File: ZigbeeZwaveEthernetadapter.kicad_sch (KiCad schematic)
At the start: 10 parts, among them J1 Barrel_Jack, J11 Conn_02x06_Odd_Even, J12 Conn_01x06, J14 Conn_01x06, J2 USB_B_Micro, J21 Conn_02x05_Odd_Even, J3 USB_C_Receptacle_USB2.0, U1 L7805

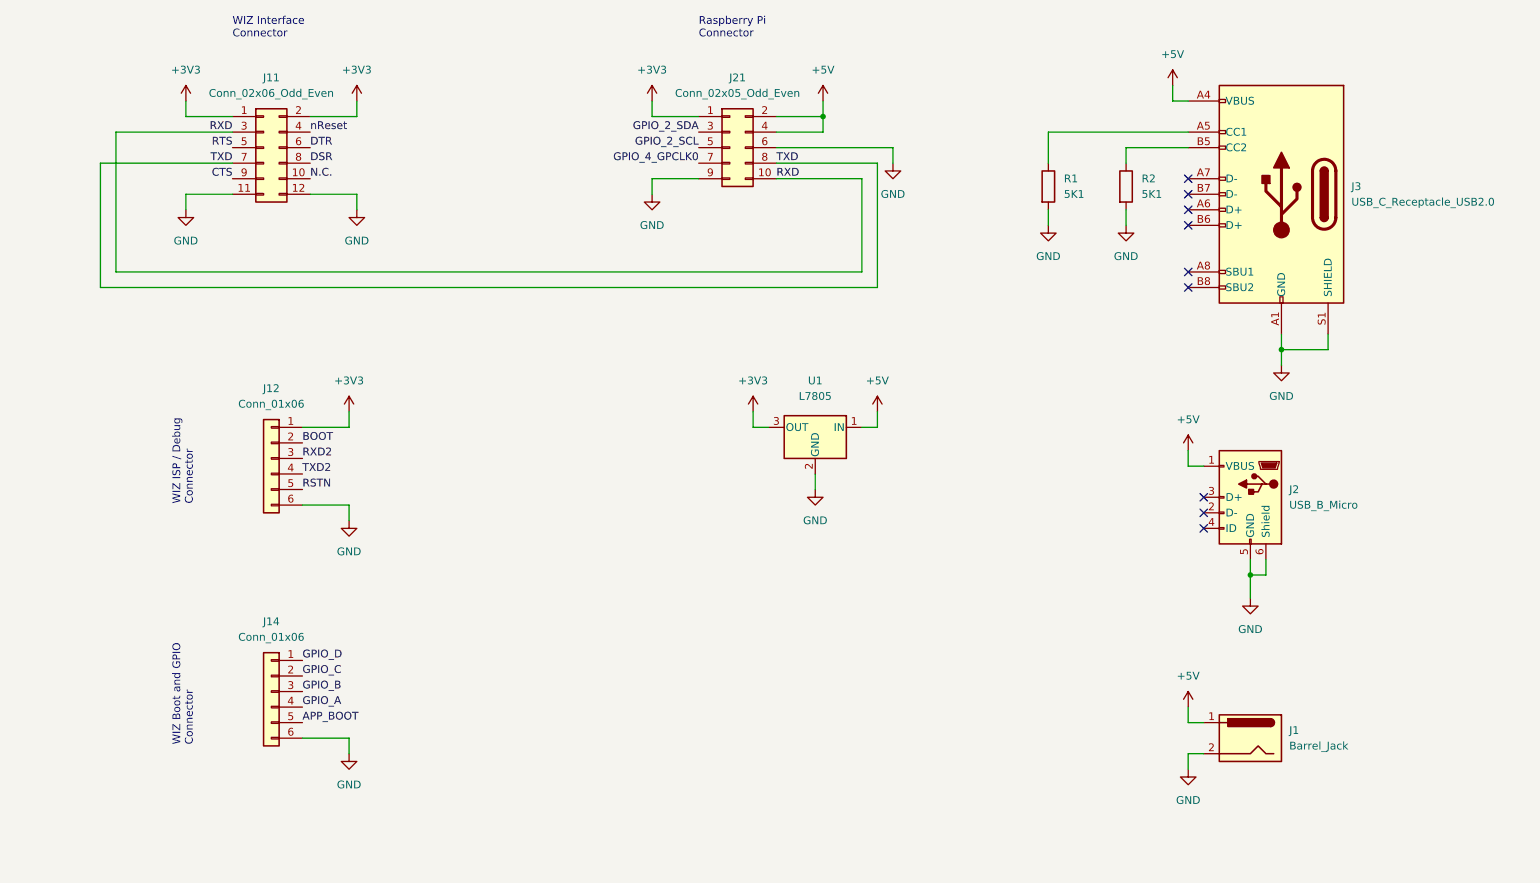
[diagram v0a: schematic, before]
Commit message: Mod: Finished schematic, changed linear regulator and added second pinout
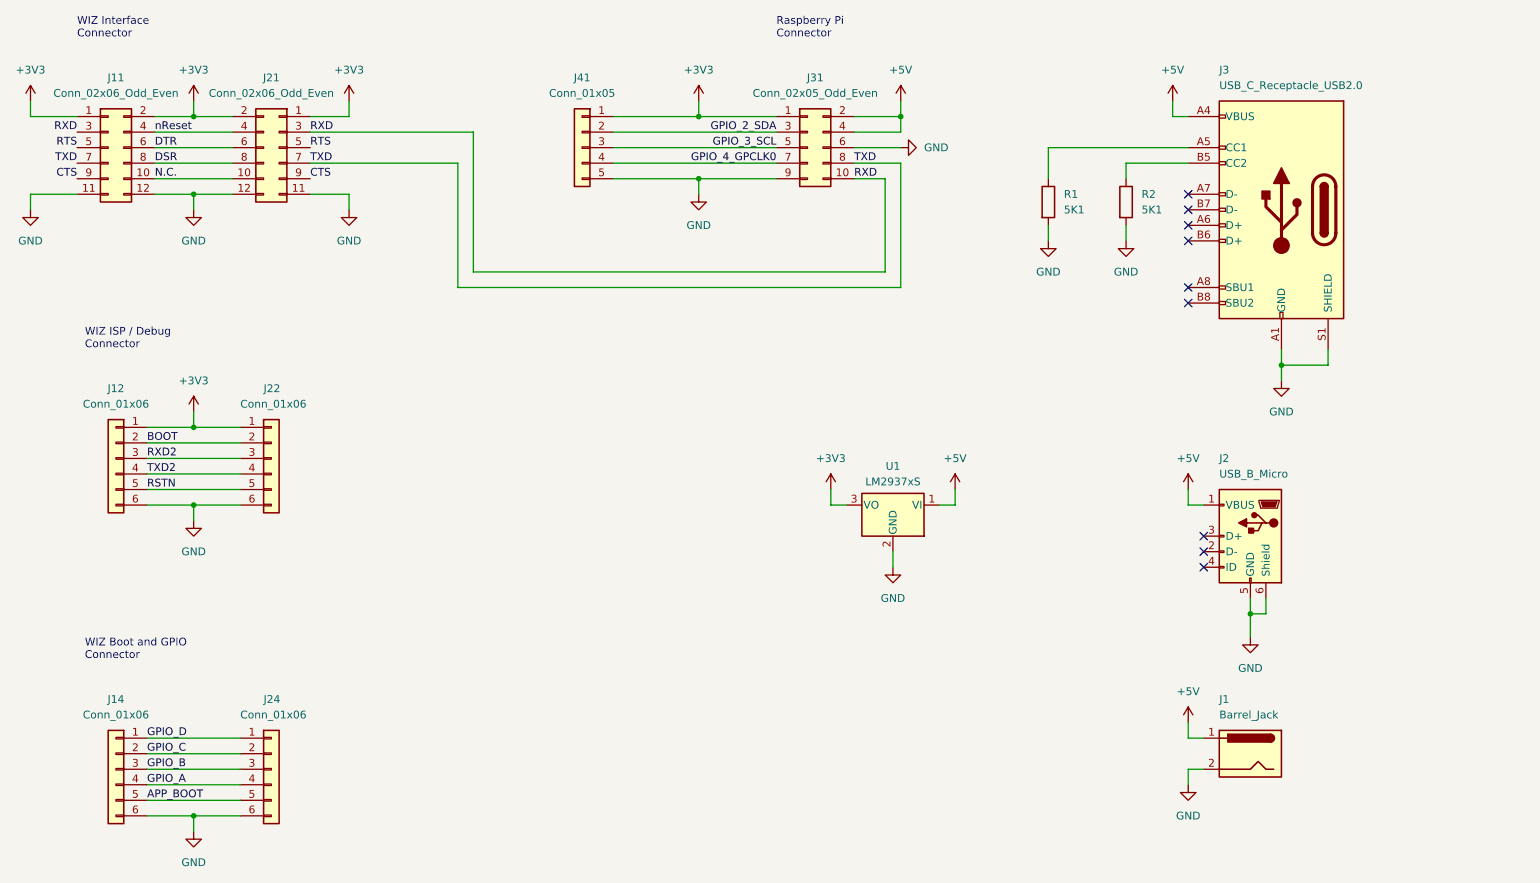
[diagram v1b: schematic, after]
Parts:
- removed U1: L7805, symbol Regulator_Linear:L7805
- added J21: Conn_02x06_Odd_Even, Connector_PinHeader_2.54mm:PinHeader_2x06_P2.54mm_Vertical, symbol Connector_Generic:Conn_02x06_Odd_Even
- added J22, J24: Conn_01x06, symbol Connector_Generic:Conn_01x06
- added J41: Conn_01x05, symbol Connector_Generic:Conn_01x05
- added U1: LM2937xS, Package_TO_SOT_SMD:TO-263-3_TabPin2, symbol Regulator_Linear:LM2937xS
- J1: footprint (none) -> Connector_BarrelJack:BarrelJack_SwitchcraftConxall_RAPC10U_Horizontal
- renumbered J21 to J31
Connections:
- net +3V3: now also J21.1 (Pin_1), J21.2 (Pin_2), J22.1 (Pin_1), J41.1 (Pin_1), U1.3 (VO)
- net +5V: now also U1.1 (VI)
- net APP_BOOT: now also J24.5 (Pin_5)
- net BOOT: now also J22.2 (Pin_2)
- net CTS: now also J21.9 (Pin_9)
- net DSR: now also J21.8 (Pin_8)
- net DTR: now also J21.6 (Pin_6)
- net GND: now also J21.11 (Pin_11), J21.12 (Pin_12), J22.6 (Pin_6), J24.6 (Pin_6), J41.5 (Pin_5), U1.2 (GND)
- net GPIO_2_SDA: now also J41.2 (Pin_2)
- net GPIO_4_GPCLK0: now also J41.4 (Pin_4)
- net GPIO_A: now also J24.4 (Pin_4)
- net GPIO_B: now also J24.3 (Pin_3)
- net GPIO_C: now also J24.2 (Pin_2)
- net GPIO_D: now also J24.1 (Pin_1)
- net N.C.: now also J21.10 (Pin_10)
- net RSTN: now also J22.5 (Pin_5)
- net RTS: now also J21.5 (Pin_5)
- net RXD: now also J21.3 (Pin_3)
- net RXD2: now also J22.3 (Pin_3)
- net TXD: now also J21.7 (Pin_7)
- net TXD2: now also J22.4 (Pin_4)
- net nReset: now also J21.4 (Pin_4)
- net GPIO_2_SCL renamed GPIO_3_SCL
- net GPIO_3_SCL: now also J41.3 (Pin_3)
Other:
- moved on the sheet: J1, J11, J12, J14, J2, J3, J31, R1, R2

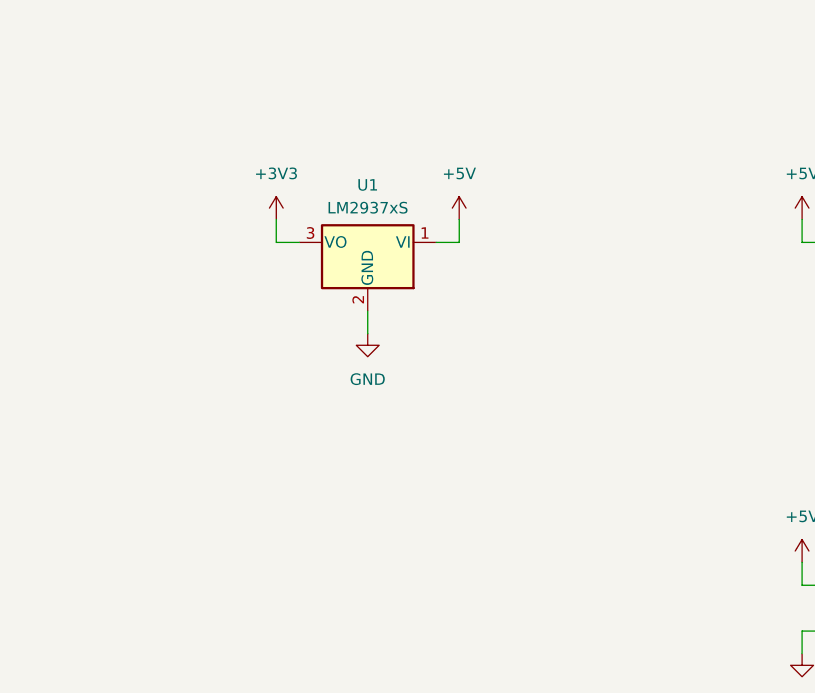
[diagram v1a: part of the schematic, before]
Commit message: Mod: LDO (U1) from LM2940 to LM3940
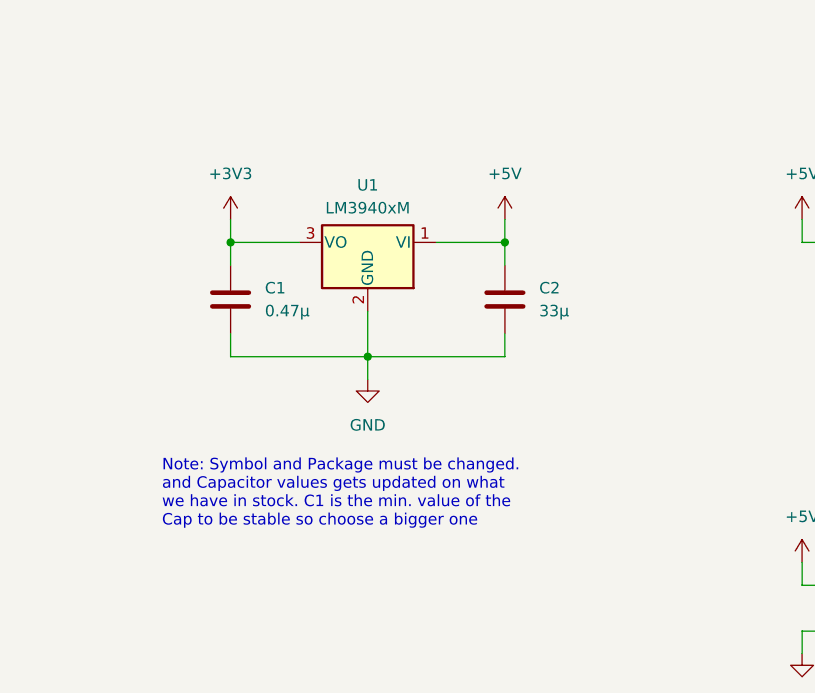
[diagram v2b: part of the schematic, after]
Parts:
- added C1: 0.47µ, symbol Device:C
- added C2: 33µ, symbol Device:C
- U1: value LM2937xS -> LM3940xM; footprint Package_TO_SOT_SMD:TO-263-3_TabPin2 -> (none)
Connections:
- net +3V3: now also C1.1
- net +5V: now also C2.1
- net GND: now also C1.2, C2.2
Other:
- note added: "Note: Symbol and Package must be changed. and Capacitor values gets updated on what we have in stock. C1 is the min. value of the Cap to be stable so choose a bigger one"
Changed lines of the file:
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@@
     (comment 4 "https://creativecommons.org/licenses/by-nc/4.0/")
   )
+  (junction (at 162.56 101.6) (diameter 0) (color 0 0 0 0)
+  )
+  (junction (at 177.8 114.3) (diameter 0) (color 0 0 0 0)
+  )
   (junction (at 63.5 38.1) (diameter 0) (color 0 0 0 0)
   )
@@
   )
   (junction (at 63.5 88.9) (diameter 0) (color 0 0 0 0)
+  )
+  (junction (at 193.04 101.6) (diameter 0) (color 0 0 0 0)
   )
   (junction (at 146.05 48.26) (diameter 0) (color 0 0 0 0)
@@
     (stroke (width 0) (type default) (color 0 0 0 0))
   )
+  (wire (pts (xy 193.04 111.76) (xy 193.04 114.3))
+    (stroke (width 0) (type default) (color 0 0 0 0))
+  )
   (wire (pts (xy 226.06 43.18) (xy 203.2 43.18))
     (stroke (width 0) (type default) (color 0 0 0 0))
@@
     (stroke (width 0) (type default) (color 0 0 0 0))
   )
+  (wire (pts (xy 162.56 114.3) (xy 177.8 114.3))
+    (stroke (width 0) (type default) (color 0 0 0 0))
+  )
   (wire (pts (xy 226.06 139.7) (xy 228.6 139.7))
     (stroke (width 0) (type default) (color 0 0 0 0))
   )
-  (wire (pts (xy 167.64 101.6) (xy 170.18 101.6))
+  (wire (pts (xy 162.56 101.6) (xy 170.18 101.6))
     (stroke (width 0) (type default) (color 0 0 0 0))
   )
@@
     (stroke (width 0) (type default) (color 0 0 0 0))
   )
-  (wire (pts (xy 167.64 99.06) (xy 167.64 101.6))
+  (wire (pts (xy 162.56 99.06) (xy 162.56 101.6))
     (stroke (width 0) (type default) (color 0 0 0 0))
   )
@@
     (stroke (width 0) (type default) (color 0 0 0 0))
   )
+  (wire (pts (xy 193.04 101.6) (xy 193.04 104.14))
+    (stroke (width 0) (type default) (color 0 0 0 0))
+  )
   (wire (pts (xy 236.22 116.84) (xy 236.22 119.38))
     (stroke (width 0) (type default) (color 0 0 0 0))
@@
     (stroke (width 0) (type default) (color 0 0 0 0))
   )
-  (wire (pts (xy 187.96 101.6) (xy 187.96 99.06))
+  (wire (pts (xy 193.04 101.6) (xy 193.04 99.06))
     (stroke (width 0) (type default) (color 0 0 0 0))
   )
@@
     (stroke (width 0) (type default) (color 0 0 0 0))
   )
+  (wire (pts (xy 177.8 114.3) (xy 177.8 116.84))
+    (stroke (width 0) (type default) (color 0 0 0 0))
+  )
   (wire (pts (xy 236.22 119.38) (xy 236.22 123.19))
     (stroke (width 0) (type default) (color 0 0 0 0))
@@
     (stroke (width 0) (type default) (color 0 0 0 0))
   )
-  (wire (pts (xy 185.42 101.6) (xy 187.96 101.6))
+  (wire (pts (xy 185.42 101.6) (xy 193.04 101.6))
+    (stroke (width 0) (type default) (color 0 0 0 0))
+  )
+  (wire (pts (xy 193.04 114.3) (xy 177.8 114.3))
     (stroke (width 0) (type default) (color 0 0 0 0))
   )
@@
     (stroke (width 0) (type default) (color 0 0 0 0))
   )
-  (wire (pts (xy 177.8 109.22) (xy 177.8 111.76))
+  (wire (pts (xy 162.56 111.76) (xy 162.56 114.3))
     (stroke (width 0) (type default) (color 0 0 0 0))
   )
@@
     (stroke (width 0) (type default) (color 0 0 0 0))
   )
+  (wire (pts (xy 177.8 109.22) (xy 177.8 114.3))
+    (stroke (width 0) (type default) (color 0 0 0 0))
+  )
   (wire (pts (xy 146.05 48.26) (xy 146.05 50.8))
     (stroke (width 0) (type default) (color 0 0 0 0))
@@
     (stroke (width 0) (type default) (color 0 0 0 0))
   )
+  (wire (pts (xy 162.56 101.6) (xy 162.56 104.14))
+    (stroke (width 0) (type default) (color 0 0 0 0))
+  )
   (wire (pts (xy 57.15 45.72) (xy 69.85 45.72))
     (stroke (width 0) (type default) (color 0 0 0 0))
@@
   )
   (text "WIZ Boot and GPIO\nConnector" (at 45.72 127 0)
+    (effects (font (size 1.27 1.27)) (justify left bottom))
+  )
+  (text "Note: Symbol and Package must be changed.\nand Capacitor values gets updated on what\nwe have in stock. C1 is the min. value of the\nCap to be stable so choose a bigger one"
+    (at 154.94 133.35 0)
     (effects (font (size 1.27 1.27)) (justify left bottom))
   )
@@
     )
     (pin "1")
+  )
+  (symbol (lib_id "Device:C") (at 193.04 107.95 0) (unit 1)
+    (in_bom yes) (on_board yes) (fields_autoplaced)
+    (property "Reference" "C2" (id 0) (at 196.85 106.6799 0)
+      (effects (font (size 1.27 1.27)) (justify left))
+    )
+    (property "Value" "33µ" (id 1) (at 196.85 109.2199 0)
+      (effects (font (size 1.27 1.27)) (justify left))
+    )
+    (property "Footprint" "" (id 2) (at 194.0052 111.76 0)
+      (effects (font (size 1.27 1.27)) hide)
+    )
+    (property "Datasheet" "~" (id 3) (at 193.04 107.95 0)
+      (effects (font (size 1.27 1.27)) hide)
+    )
+    (pin "1")
+    (pin "2")
   )
   (symbol (lib_id "Connector:USB_B_Micro") (at 236.22 106.68 0) (mirror y) (unit 1)
@@
     (pin "6")
   )
-  (symbol (lib_id "power:GND") (at 177.8 111.76 0) (unit 1)
-    (in_bom yes) (on_board yes) (fields_autoplaced)
-    (property "Reference" "#PWR017" (id 0) (at 177.8 118.11 0)
-      (effects (font (size 1.27 1.27)) hide)
-    )
-    (property "Value" "GND" (id 1) (at 177.8 116.84 0))
-    (property "Footprint" "" (id 2) (at 177.8 111.76 0)
-      (effects (font (size 1.27 1.27)) hide)
-    )
-    (property "Datasheet" "" (id 3) (at 177.8 111.76 0)
+  (symbol (lib_id "power:GND") (at 177.8 116.84 0) (unit 1)
+    (in_bom yes) (on_board yes) (fields_autoplaced)
+    (property "Reference" "#PWR017" (id 0) (at 177.8 123.19 0)
+      (effects (font (size 1.27 1.27)) hide)
+    )
+    (property "Value" "GND" (id 1) (at 177.8 121.92 0))
+    (property "Footprint" "" (id 2) (at 177.8 116.84 0)
+      (effects (font (size 1.27 1.27)) hide)
+    )
+    (property "Datasheet" "" (id 3) (at 177.8 116.84 0)
       (effects (font (size 1.27 1.27)) hide)
     )
@@
     (in_bom yes) (on_board yes)
     (property "Reference" "U1" (id 0) (at 177.8 95.25 0))
-    (property "Value" "LM2937xS" (id 1) (at 177.8 97.79 0))
-    (property "Footprint" "Package_TO_SOT_SMD:TO-263-3_TabPin2" (id 2) (at 177.8 95.885 0)
+    (property "Value" "LM3940xM" (id 1) (at 177.8 97.79 0))
+    (property "Footprint" "" (id 2) (at 177.8 95.885 0)
       (effects (font (size 1.27 1.27) italic) hide)
     )
-    (property "Datasheet" "http://www.ti.com/lit/ds/symlink/lm2937.pdf" (id 3) (at 177.8 102.87 0)
+    (property "Datasheet" "" (id 3) (at 177.8 102.87 0)
       (effects (font (size 1.27 1.27)) hide)
     )
@@
     (pin "1")
   )
-  (symbol (lib_id "power:+3V3") (at 167.64 99.06 0) (unit 1)
-    (in_bom yes) (on_board yes) (fields_autoplaced)
-    (property "Reference" "#PWR014" (id 0) (at 167.64 102.87 0)
-      (effects (font (size 1.27 1.27)) hide)
-    )
-    (property "Value" "+3V3" (id 1) (at 167.64 93.98 0))
-    (property "Footprint" "" (id 2) (at 167.64 99.06 0)
-      (effects (font (size 1.27 1.27)) hide)
-    )
-    (property "Datasheet" "" (id 3) (at 167.64 99.06 0)
+  (symbol (lib_id "power:+3V3") (at 162.56 99.06 0) (unit 1)
+    (in_bom yes) (on_board yes) (fields_autoplaced)
+    (property "Reference" "#PWR014" (id 0) (at 162.56 102.87 0)
+      (effects (font (size 1.27 1.27)) hide)
+    )
+    (property "Value" "+3V3" (id 1) (at 162.56 93.98 0))
+    (property "Footprint" "" (id 2) (at 162.56 99.06 0)
+      (effects (font (size 1.27 1.27)) hide)
+    )
+    (property "Datasheet" "" (id 3) (at 162.56 99.06 0)
       (effects (font (size 1.27 1.27)) hide)
     )
@@
     (pin "1")
   )
-  (symbol (lib_id "power:+5V") (at 187.96 99.06 0) (unit 1)
-    (in_bom yes) (on_board yes) (fields_autoplaced)
-    (property "Reference" "#PWR015" (id 0) (at 187.96 102.87 0)
-      (effects (font (size 1.27 1.27)) hide)
-    )
-    (property "Value" "+5V" (id 1) (at 187.96 93.98 0))
-    (property "Footprint" "" (id 2) (at 187.96 99.06 0)
-      (effects (font (size 1.27 1.27)) hide)
-    )
-    (property "Datasheet" "" (id 3) (at 187.96 99.06 0)
+  (symbol (lib_id "power:+5V") (at 193.04 99.06 0) (unit 1)
+    (in_bom yes) (on_board yes) (fields_autoplaced)
+    (property "Reference" "#PWR015" (id 0) (at 193.04 102.87 0)
+      (effects (font (size 1.27 1.27)) hide)
+    )
+    (property "Value" "+5V" (id 1) (at 193.04 93.98 0))
+    (property "Footprint" "" (id 2) (at 193.04 99.06 0)
+      (effects (font (size 1.27 1.27)) hide)
+    )
+    (property "Datasheet" "" (id 3) (at 193.04 99.06 0)
       (effects (font (size 1.27 1.27)) hide)
     )
@@
     (pin "5")
     (pin "6")
+  )
+  (symbol (lib_id "Device:C") (at 162.56 107.95 0) (unit 1)
+    (in_bom yes) (on_board yes) (fields_autoplaced)
+    (property "Reference" "C1" (id 0) (at 166.37 106.6799 0)
+      (effects (font (size 1.27 1.27)) (justify left))
+    )
+    (property "Value" "0.47µ" (id 1) (at 166.37 109.2199 0)
+      (effects (font (size 1.27 1.27)) (justify left))
+    )
+    (property "Footprint" "" (id 2) (at 163.5252 111.76 0)
+      (effects (font (size 1.27 1.27)) hide)
+    )
+    (property "Datasheet" "~" (id 3) (at 162.56 107.95 0)
+      (effects (font (size 1.27 1.27)) hide)
+    )
+    (pin "1")
+    (pin "2")
   )
   (symbol (lib_id "Device:R") (at 203.2 52.07 0) (unit 1)
@@
       (reference "#PWR024") (unit 1) (value "GND") (footprint "")
     )
+    (path "/ce9a570a-5e1a-4650-bd4b-81e7c520e33e"
+      (reference "C1") (unit 1) (value "0.47µ") (footprint "")
+    )
+    (path "/0b2d7c04-7285-40e3-810d-442abf84c149"
+      (reference "C2") (unit 1) (value "33µ") (footprint "")
+    )
     (path "/45ccafcf-91a6-475a-88ef-bc1903af912b"
       (reference "J1") (unit 1) (value "Barrel_Jack") (footprint "Connector_BarrelJack:BarrelJack_SwitchcraftConxall_RAPC10U_Horizontal")
@@
     )
     (path "/275839e4-00de-4be8-83f2-680a421afcba"
-      (reference "U1") (unit 1) (value "LM2937xS") (footprint "Package_TO_SOT_SMD:TO-263-3_TabPin2")
-    )
-  )
+      (reference "U1") (unit 1) (value "LM3940xM") (footprint "")
+    )
+  )

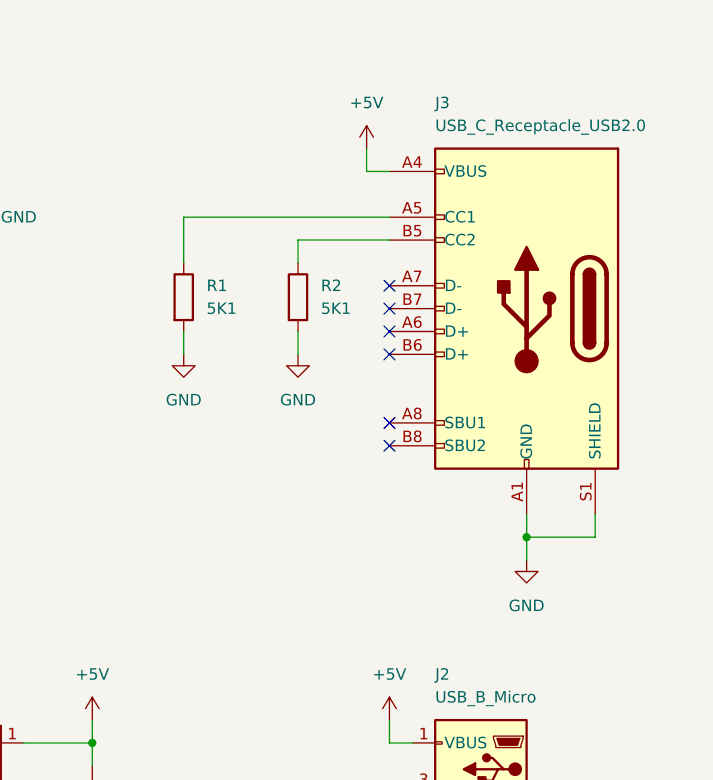
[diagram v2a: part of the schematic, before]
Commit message: Mod: Symbol from USB Type-C receptacle and assigned footprint
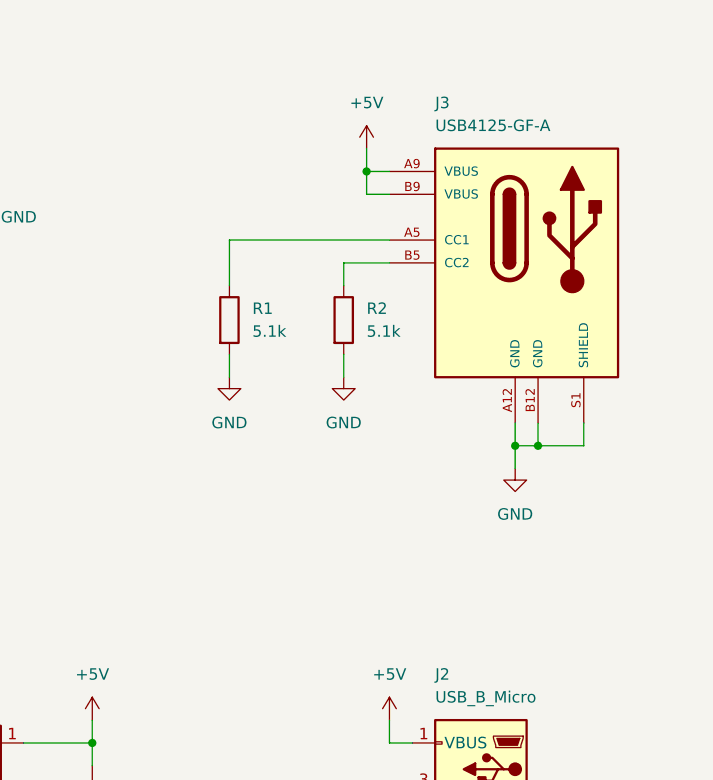
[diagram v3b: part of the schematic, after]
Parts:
- removed J3: USB_C_Receptacle_USB2.0, symbol Connector:USB_C_Receptacle_USB2.0
- added J3: USB4125-GF-A, ZigbeeZwaveEthernetadapter:GCT_USB4125-GF-A, symbol ZigbeeZwaveEthernetadapter:USB4125-GF-A
- R1, R2: value 5K1 -> 5.1k
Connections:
- net +5V: now also J3.A9 (VBUS), J3.B9 (VBUS)
- net GND: now also J3.A12 (GND), J3.B12 (GND), J3.S1 (SHIELD)
- net at R1.1: now also J3.A5 (CC1)
- net at R2.1: now also J3.B5 (CC2)
- no-connect marks 9 -> 3
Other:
- moved on the sheet: R1, R2
